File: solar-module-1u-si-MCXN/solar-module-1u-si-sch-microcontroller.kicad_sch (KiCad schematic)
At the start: 50 parts, among them J15 2X1_TH_JUMPER, J3 OreSat Debug, U1 MCXN947VKLT, U11 TCAN330, U2 TMP101NA/3KSLOTTED, U7 TMP101NA/3KSLOTTED, Y1 32.768 KHz, Y2 24 MHz

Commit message: Fixed ERC errors, including unused blocks and some power stuff.
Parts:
- removed C5, C9: 4.7p, oresat-passives:0603-C-NOSILK, symbol Device:C_Small
- removed J15: 2X1_TH_JUMPER, oresat-live-card:2X1, symbol Jumper:Jumper_2_Open
- removed TP26, TP27, TP28, TP29, TP4, TP7: Test-Point, oresat-misc:TestPoint-0.75mm-th, symbol oresat-misc:Test-Point-0.75mm-th
- removed Y1: 32.768 KHz, Crystal:Crystal_SMD_3215-2Pin_3.2x1.5mm, symbol Device:Crystal_Small
- added J2: Conn_01x02, Connector_PinHeader_2.54mm:PinHeader_1x02_P2.54mm_Vertical, symbol Connector_Generic:Conn_01x02
- added unit 5 of U1
- added unit 4 of U1
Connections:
- net GND: now also J2.2 (Pin_2)
- net at R9.1, U1.82 (P0_6): now also J2.1 (Pin_1)
- net VBUS: no longer names the net of J3.1 (VBUSP), J3.2 (VBUSP)
- no-connect marks 40 -> 70
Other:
- note added: "OreSat Debug"
- note added: "VDD_BAT"
- moved on the sheet: C1, C11, C16, C25, C26, C27, C28, C29, C3, C30, C31, C46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

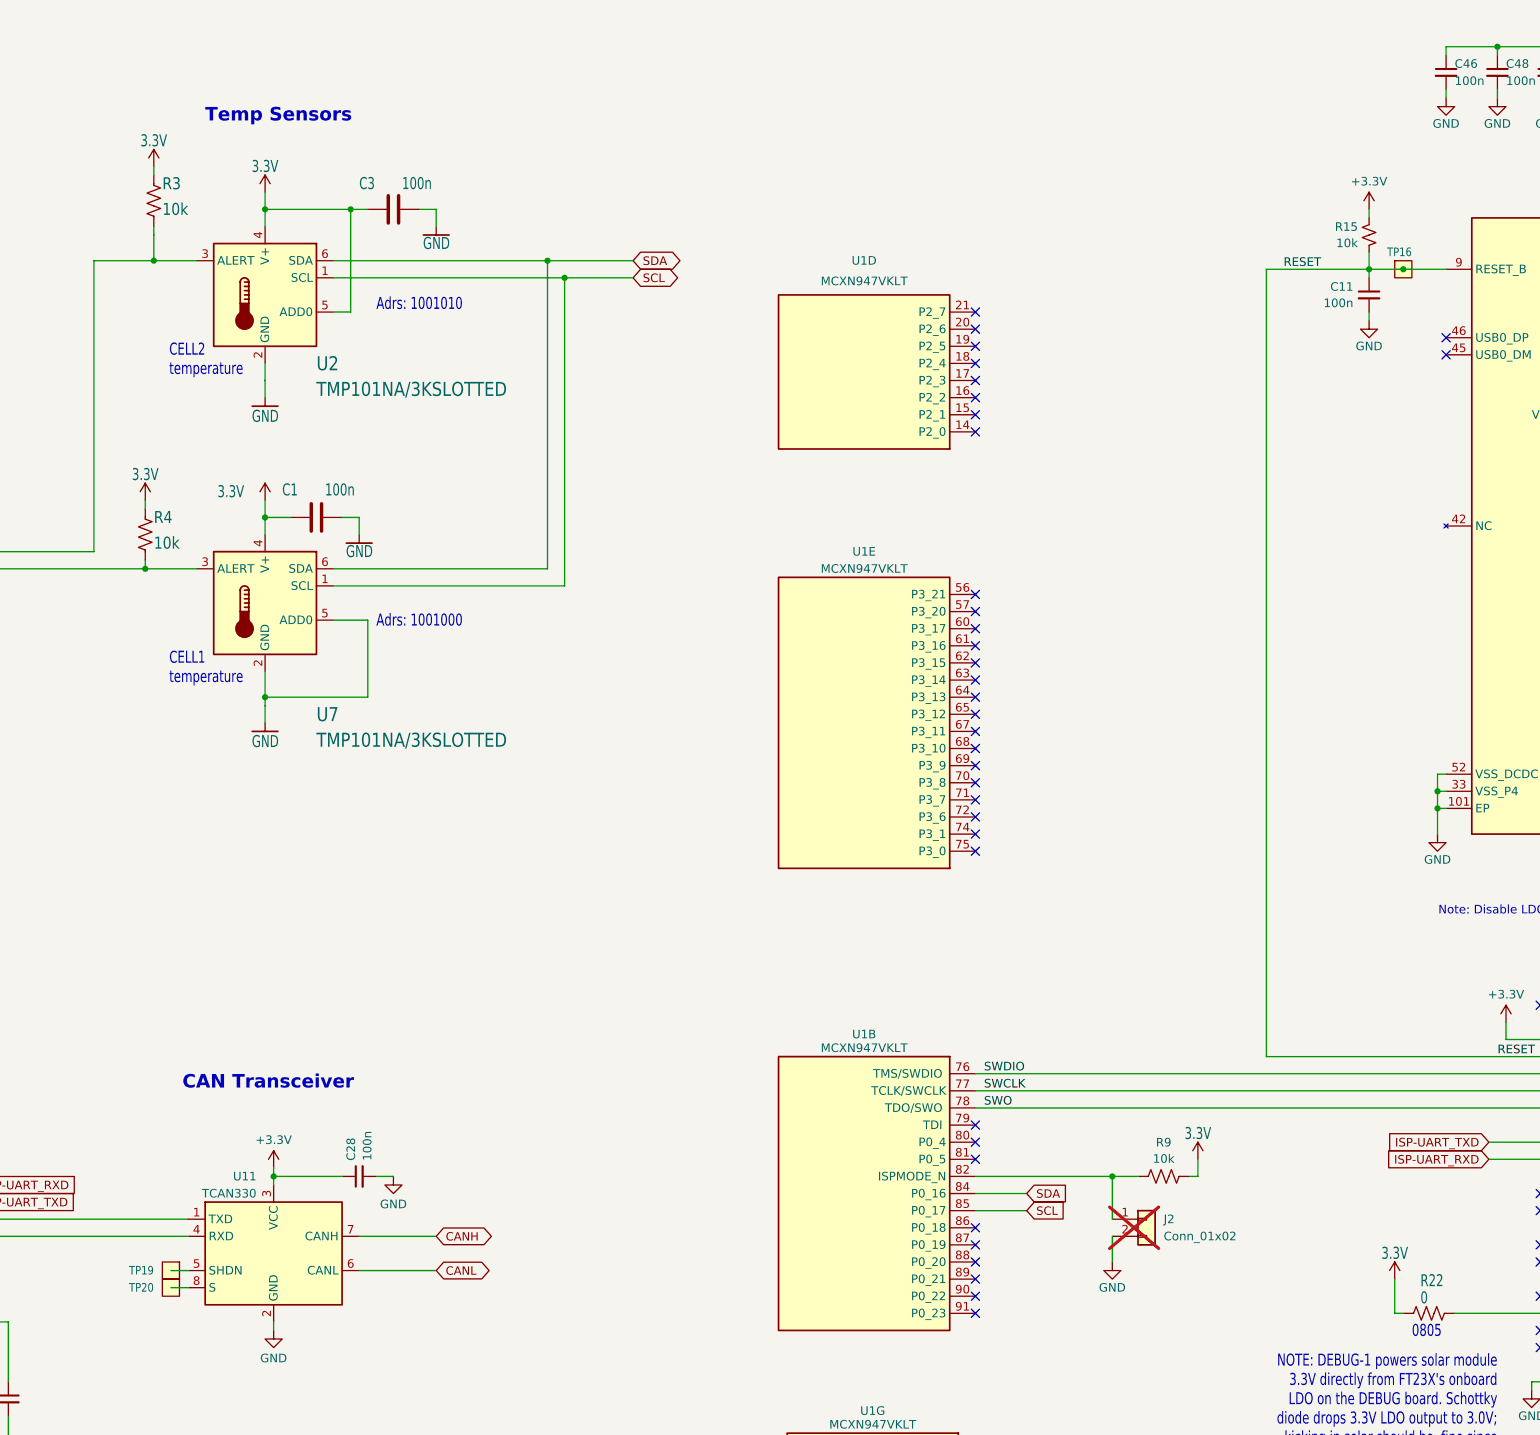
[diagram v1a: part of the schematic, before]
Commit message: moved to 4 layer board and added MCXN to PCB, some routing started
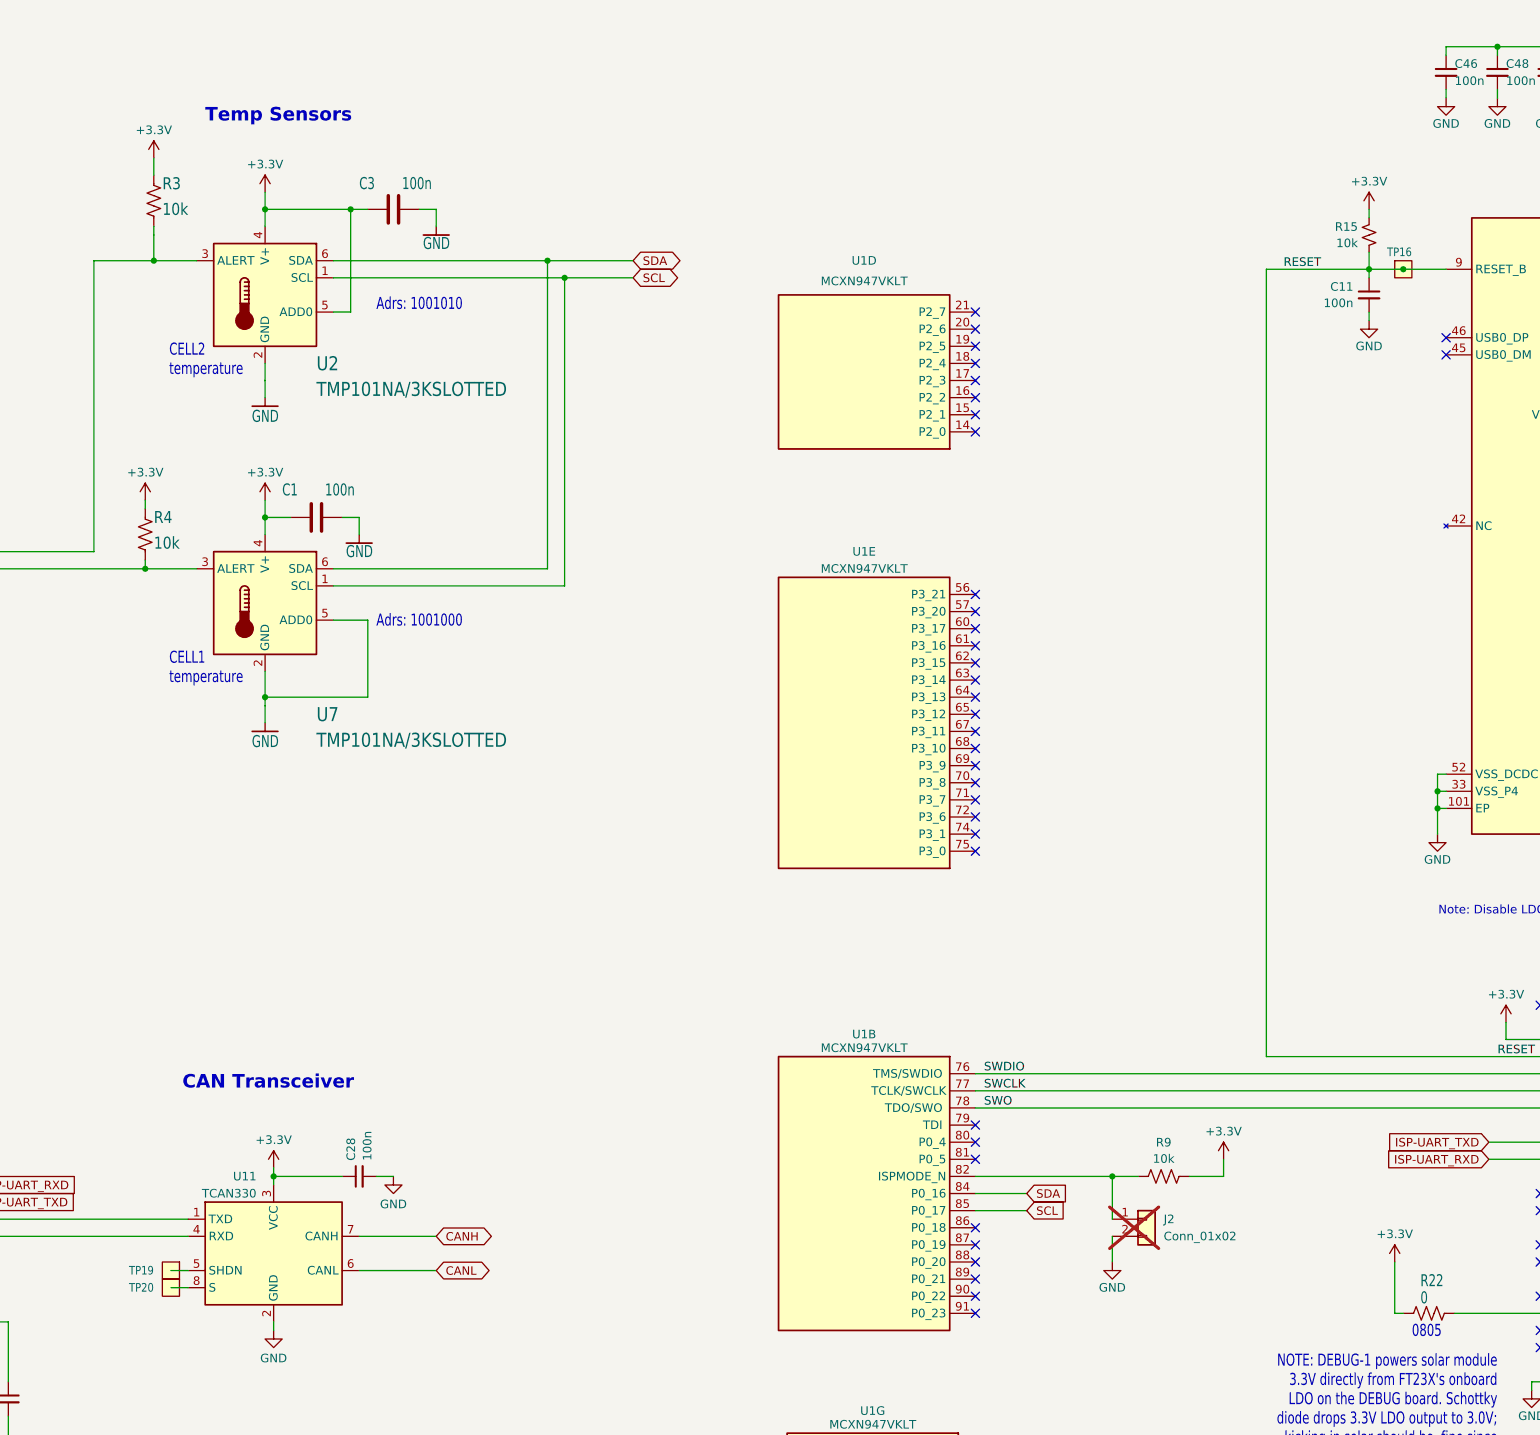
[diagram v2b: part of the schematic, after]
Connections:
- net 3.3V is gone; now on net +3.3V: C1.1, C3.1, R22.2, R3.2, R4.2, R9.2, U2.4 (V+), U2.5 (ADD0), U7.4 (V+)

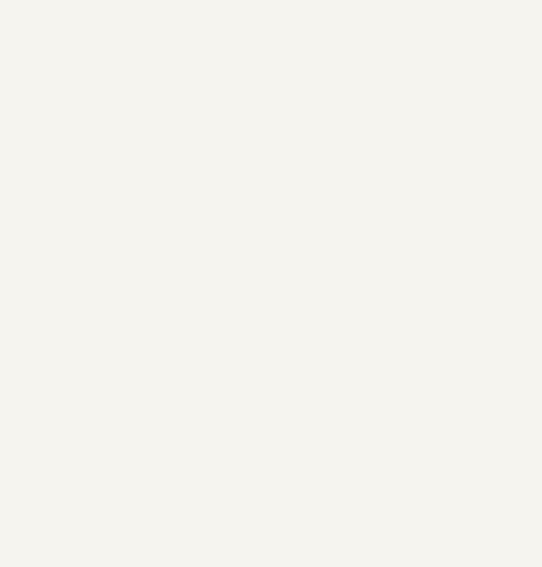
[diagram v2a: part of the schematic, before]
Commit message: More routing work, pulled power routing onto another layer
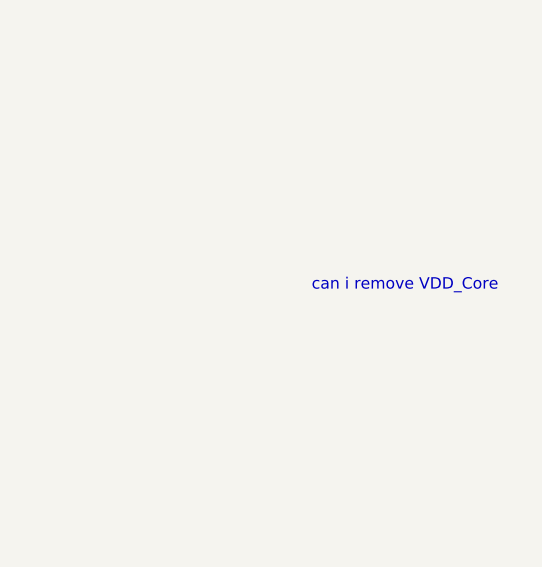
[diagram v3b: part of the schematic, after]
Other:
- note added: "can i remove VDD_Core"
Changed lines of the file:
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@@
+		)
+	)
+	(text "can i remove VDD_Core"
+		(exclude_from_sim no)
+		(at 466.598 97.79 0)
+		(effects
+			(font
+				(size 1.27 1.27)
+			)
 		)
 	)

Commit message: more layout and routing
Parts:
- R9: footprint (none) -> oresat-passives:0603-C-NOSILK
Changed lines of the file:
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@@
 			)
 		)
-		(property "Footprint" ""
+		(property "Footprint" "oresat-passives:0603-C-NOSILK"
 			(at 288.544 189.484 90)
 			(effects

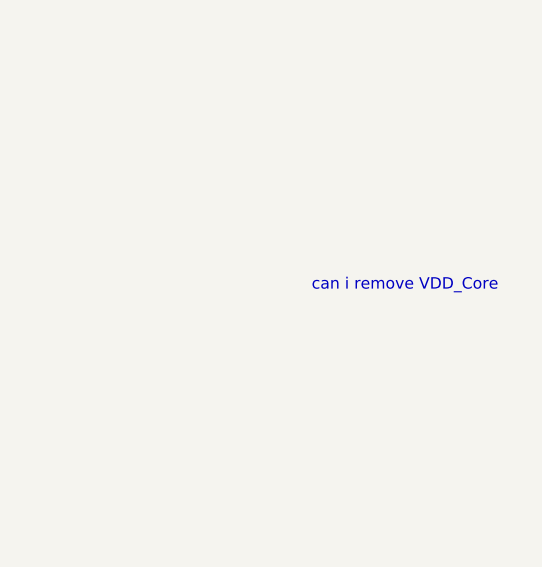
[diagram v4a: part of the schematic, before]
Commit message: Finished routing, starting on fixing DRC
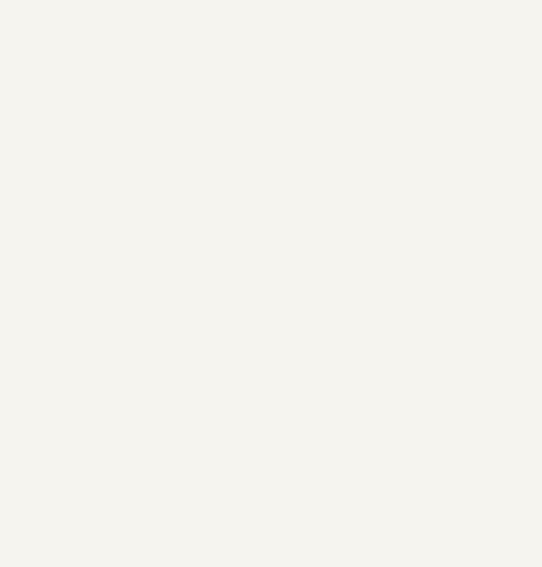
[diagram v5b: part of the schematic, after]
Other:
- note removed: "can i remove VDD_Core"
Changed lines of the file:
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@@
-		)
-	)
-	(text "can i remove VDD_Core"
-		(exclude_from_sim no)
-		(at 466.598 97.79 0)
-		(effects
-			(font
-				(size 1.27 1.27)
-			)
 		)
 	)

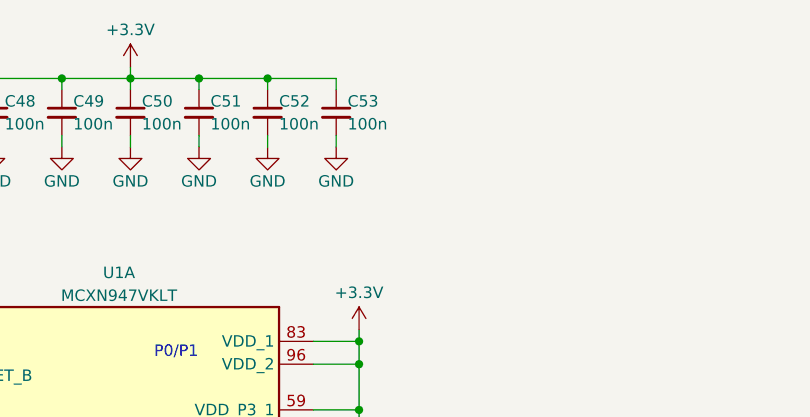
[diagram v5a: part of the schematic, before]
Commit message: redid all routing to MXCN with added capacitors
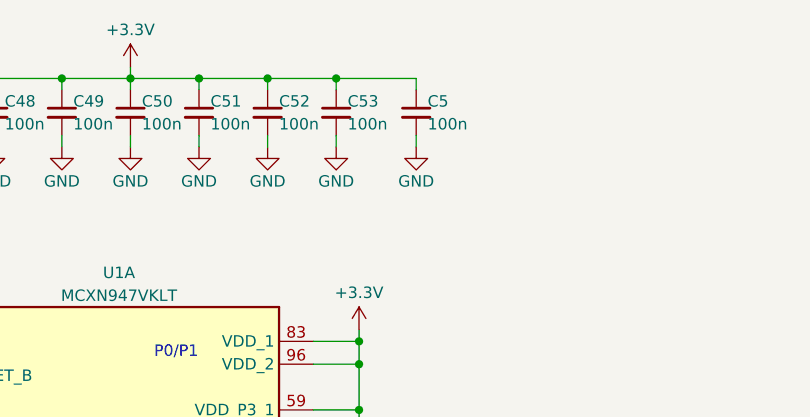
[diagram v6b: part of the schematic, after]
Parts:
- added C5: 100n, oresat-passives:0603-C-NOSILK, symbol Device:C_Small
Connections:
- net +3.3V: now also C5.1
- net GND: now also C5.2
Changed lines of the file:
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@@
 	)
 	(junction
+		(at 375.92 22.86)
+		(diameter 0)
+		(color 0 0 0 0)
+	)
+	(junction
 		(at 104.14 191.77)
 		(diameter 0)
@@
 	(wire
 		(pts
+			(xy 384.81 29.21) (xy 384.81 30.48)
+		)
+		(stroke
+			(width 0)
+			(type default)
+		)
+	)
+	(wire
+		(pts
 			(xy 143.51 199.39) (xy 93.98 199.39)
 		)
@@
 	(wire
 		(pts
+			(xy 384.81 24.13) (xy 384.81 22.86)
+		)
+		(stroke
+			(width 0)
+			(type default)
+		)
+	)
+	(wire
+		(pts
 			(xy 154.94 92.71) (xy 154.94 95.25)
 		)
@@
 	(wire
 		(pts
+			(xy 384.81 22.86) (xy 375.92 22.86)
+		)
+		(stroke
+			(width 0)
+			(type default)
+		)
+	)
+	(wire
+		(pts
 			(xy 330.2 22.86) (xy 337.82 22.86)
 		)
@@
 	(symbol
 		(lib_id "power:GND")
+		(at 384.81 30.48 0)
+		(unit 1)
+		(exclude_from_sim no)
+		(in_bom yes)
+		(on_board yes)
+		(dnp no)
+		(property "Reference" "#PWR059"
+			(at 384.81 36.83 0)
+			(effects
+				(font
+					(size 1.27 1.27)
+				)
+				(hide yes)
+			)
+		)
+		(property "Value" "GND"
+			(at 384.81 34.29 0)
+			(effects
+				(font
+					(size 1.27 1.27)
+				)
+			)
+		)
+		(property "Footprint" ""
+			(at 384.81 30.48 0)
+			(effects
+				(font
+					(size 1.27 1.27)
+				)
+				(hide yes)
+			)
+		)
+		(property "Datasheet" ""
+			(at 384.81 30.48 0)
+			(effects
+				(font
+					(size 1.27 1.27)
+				)
+				(hide yes)
+			)
+		)
+		(property "Description" "Power symbol creates a global label with name \"GND\" , ground"
+			(at 384.81 30.48 0)
+			(effects
+				(font
+					(size 1.27 1.27)
+				)
+				(hide yes)
+			)
+		)
+		(pin "1"
+		)
+		(instances
+			(project "solar-module-1u-si"
+				(path "/115bd2cd-7c08-4b54-867b-a326ee0699c1/bfa81e66-0bc2-4d21-a09c-e64719ae80bc"
+					(reference "#PWR059")
+					(unit 1)
+				)
+			)
+		)
+	)
+	(symbol
+		(lib_id "power:GND")
 		(at 387.35 129.54 0)
 		(mirror y)
@@
 					(unit 1)
 				)
+			)
+		)
+	)
+	(symbol
+		(lib_id "Device:C_Small")
+		(at 384.81 26.67 0)
+		(unit 1)
+		(exclude_from_sim no)
+		(in_bom yes)
+		(on_board yes)
+		(dnp no)
+		(property "Reference" "C5"
+			(at 386.08 25.4 0)
+			(effects
+				(font
+					(size 1.27 1.27)
+				)
+				(justify left)
+			)
+		)
+		(property "Value" "100n"
+			(at 386.08 27.94 0)
+			(effects
+				(font
+					(size 1.27 1.27)
+				)
+				(justify left)
+			)
+		)
+		(property "Footprint" "oresat-passives:0603-C-NOSILK"
+			(at 384.81 26.67 0)
+			(effects
+				(font
+					(size 1.27 1.27)
+				)
+				(hide yes)
+			)
+		)
+		(property "Datasheet" "https://search.murata.co.jp/Ceramy/image/img/A01X/G101/ENG/GRM188R72A104KA35-01.pdf"
+			(at 384.81 26.67 0)
+			(effects
+				(font
+					(size 1.27 1.27)
+				)
+				(hide yes)
+			)
+		)
+		(property "Description" "0.1 µF ±10% 100V Ceramic Capacitor X7R 0603 (1608 Metric)"
+			(at 384.81 26.67 0)
+			(effects
+				(font
+					(size 1.27 1.27)
+				)
+				(hide yes)
+			)
+		)
+		(property "MFR" "Murata Electronics"
+			(at 384.81 26.67 0)
+			(effects
+				(font
+					(size 1.27 1.27)
+				)
+				(hide yes)
+			)
+		)
+		(property "MPN" "GRM188R72A104KA35D"
+			(at 384.81 26.67 0)
+			(effects
+				(font
+					(size 1.27 1.27)
+				)
+				(hide yes)
+			)
+		)
+		(pin "2"
+		)
+		(pin "1"
+		)
+		(instances
+			(project "solar-module-1u-si"
+				(path "/115bd2cd-7c08-4b54-867b-a326ee0699c1/bfa81e66-0bc2-4d21-a09c-e64719ae80bc"
+					(reference "C5")
+					(unit 1)
+				)
